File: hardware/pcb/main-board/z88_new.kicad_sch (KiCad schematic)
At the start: 0 parts

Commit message: start next board iteration, add latch and pico power bits
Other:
- added sheet Picos Latch (picos_latch.kicad_sch)
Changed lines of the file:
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@@
 	(title_block
 		(title "Z88R - Z88 Recreated")
-		(date "2024-08-23")
-		(rev "20240823")
+		(date "2025-12-19")
+		(rev "20251219WIP")
 		(company "Fountain and Menadue")
 	)
@@
 				)
 			)
+		)
+	)
+	(sheet
+		(at 50.8 189.23)
+		(size 20.32 3.81)
+		(fields_autoplaced yes)
+		(stroke
+			(width 0.1524)
+			(type solid)
+		)
+		(fill
+			(color 0 0 0 0.0000)
+		)
+		(property "Sheetname" "Picos Latch"
+			(at 50.8 188.5184 0)
+			(effects
+				(font
+					(size 1.27 1.27)
+				)
+				(justify left bottom)
+			)
+		)
+		(property "Sheetfile" "picos_latch.kicad_sch"
+			(at 50.8 193.6246 0)
+			(effects
+				(font
+					(size 1.27 1.27)
+				)
+				(justify left top)
+			)
+		)
+		(instances
+			(project "z88_new"
+				(path "/fdce8012-5f35-4f58-8abb-80214b4af8fe"
+					(page "11")
+				)
+			)

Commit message: make a start on RP2040 to replace the KB pico
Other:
- added sheet KB_RP2040 (kb_rp2040.kicad_sch)
- title: Z88R - Z88 Recreated -> Z88R - Z88 Recreation
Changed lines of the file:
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@@
 	(paper "A4")
 	(title_block
-		(title "Z88R - Z88 Recreated")
-		(date "2025-12-19")
-		(rev "20251219WIP")
+		(title "Z88R - Z88 Recreation")
+		(date "2025-12-30")
+		(rev "20251230WIP")
 		(company "Fountain and Menadue")
 	)
@@
 				)
 			)
+		)
+	)
+	(sheet
+		(at 90.17 187.96)
+		(size 25.4 3.81)
+		(fields_autoplaced yes)
+		(stroke
+			(width 0.1524)
+			(type solid)
+		)
+		(fill
+			(color 0 0 0 0.0000)
+		)
+		(property "Sheetname" "KB_RP2040"
+			(at 90.17 187.2484 0)
+			(effects
+				(font
+					(size 1.27 1.27)
+				)
+				(justify left bottom)
+			)
+		)
+		(property "Sheetfile" "kb_rp2040.kicad_sch"
+			(at 90.17 192.3546 0)
+			(effects
+				(font
+					(size 1.27 1.27)
+				)
+				(justify left top)
+			)
+		)
+		(instances
+			(project "z88_new"
+				(path "/fdce8012-5f35-4f58-8abb-80214b4af8fe"
+					(page "12")
+				)
+			)

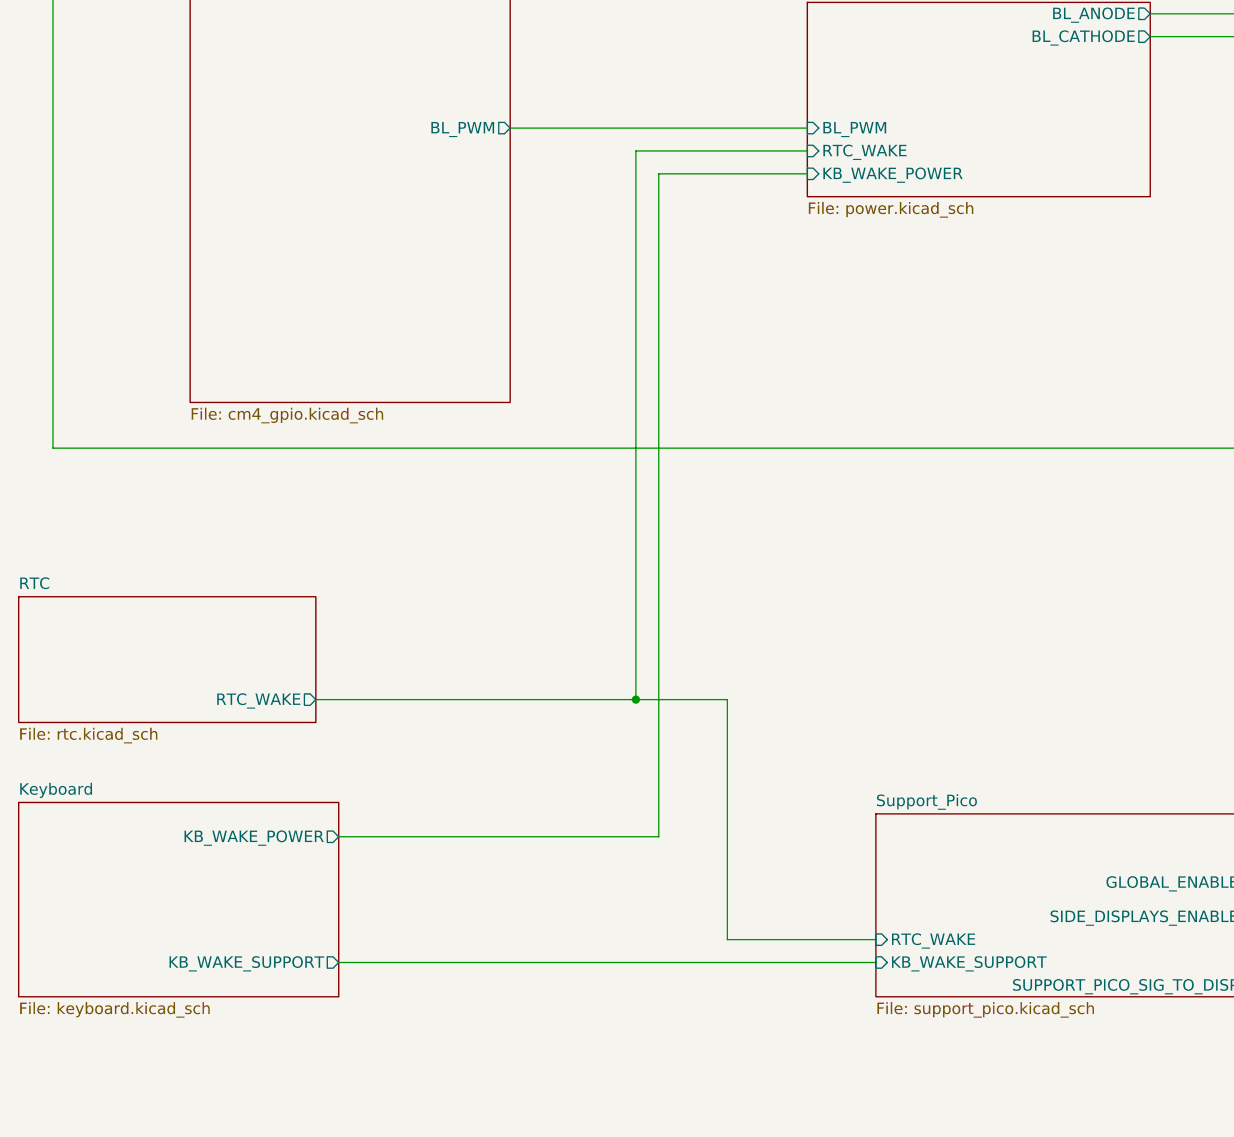
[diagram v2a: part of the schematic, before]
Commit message: more working out of the KB pico replacement
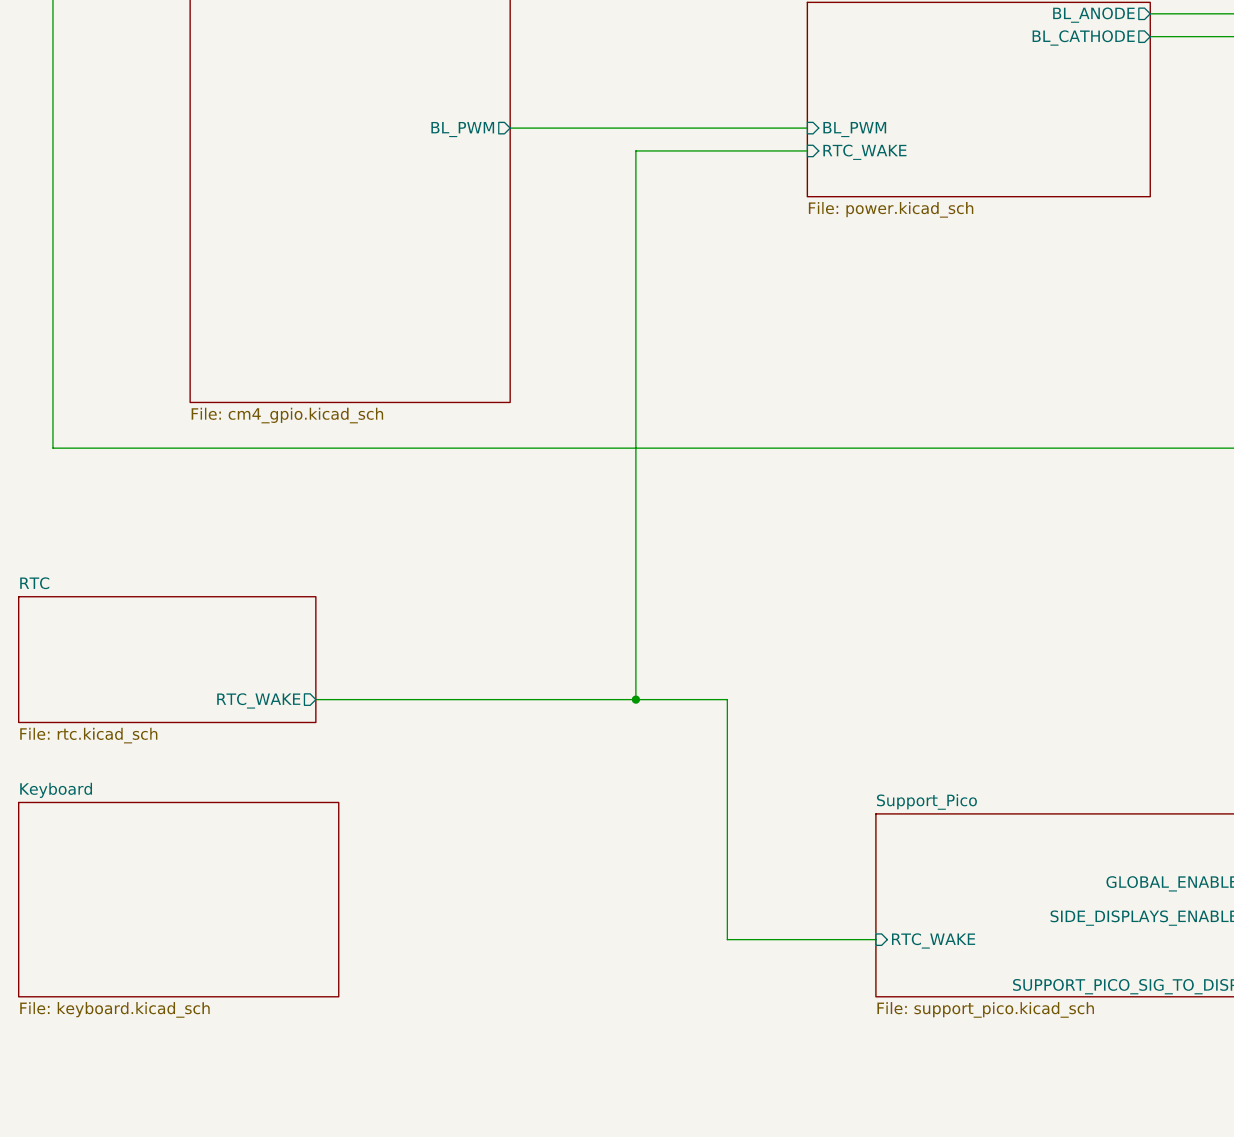
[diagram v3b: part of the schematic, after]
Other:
- sheet Keyboard ports: added none; removed KB_WAKE_POWER, KB_WAKE_SUPPORT
- sheet Power ports: added none; removed KB_WAKE_POWER
- sheet Support_Pico ports: added none; removed KB_WAKE_SUPPORT
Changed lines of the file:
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@@
-	(wire
-		(pts
-			(xy 96.52 58.42) (xy 113.03 58.42)
-		)
-		(stroke
-			(width 0)
-			(type default)
-		)
-	)
-	(wire
-		(pts
-			(xy 60.96 146.05) (xy 120.65 146.05)
-		)
-		(stroke
-			(width 0)
-			(type default)
-		)
-	)
 	(wire
 		(pts
@@
 	(wire
 		(pts
-			(xy 96.52 132.08) (xy 96.52 58.42)
-		)
-		(stroke
-			(width 0)
-			(type default)
-		)
-	)
-	(wire
-		(pts
 			(xy 104.14 143.51) (xy 120.65 143.51)
 		)
@@
 		(pts
 			(xy 93.98 55.88) (xy 93.98 116.84)
-		)
-		(stroke
-			(width 0)
-			(type default)
-		)
-	)
-	(wire
-		(pts
-			(xy 60.96 132.08) (xy 96.52 132.08)
 		)
 		(stroke
@@
 		(pin "RTC_WAKE" input
 			(at 120.65 143.51 180)
-			(effects
-				(font
-					(size 1.27 1.27)
-				)
-				(justify left)
-			)
-		)
-		(pin "KB_WAKE_SUPPORT" input
-			(at 120.65 146.05 180)
 			(effects
 				(font
@@
 			)
 		)
-		(pin "KB_WAKE_SUPPORT" output
-			(at 60.96 146.05 0)
-			(effects
-				(font
-					(size 1.27 1.27)
-				)
-				(justify right)
-			)
-		)
-		(pin "KB_WAKE_POWER" output
-			(at 60.96 132.08 0)
-			(effects
-				(font
-					(size 1.27 1.27)
-				)
-				(justify right)
-			)
-		)
 		(instances
 			(project "z88_new"
@@
 			(effects
 				(font
-					(size 1.27 1.27)
-				)
-				(justify left)
-			)
-		)
-		(pin "KB_WAKE_POWER" input
-			(at 113.03 58.42 180)
-			(effects
-				(font

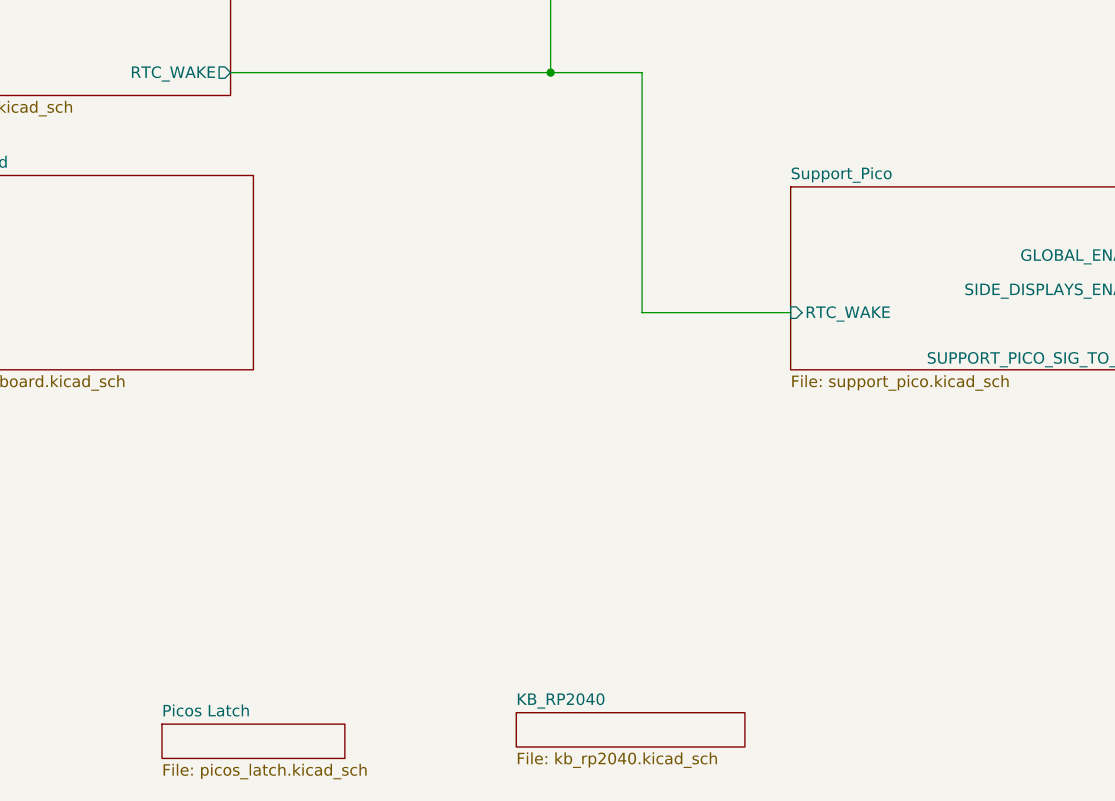
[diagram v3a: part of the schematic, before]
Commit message: start the support pico rp2040 replacement
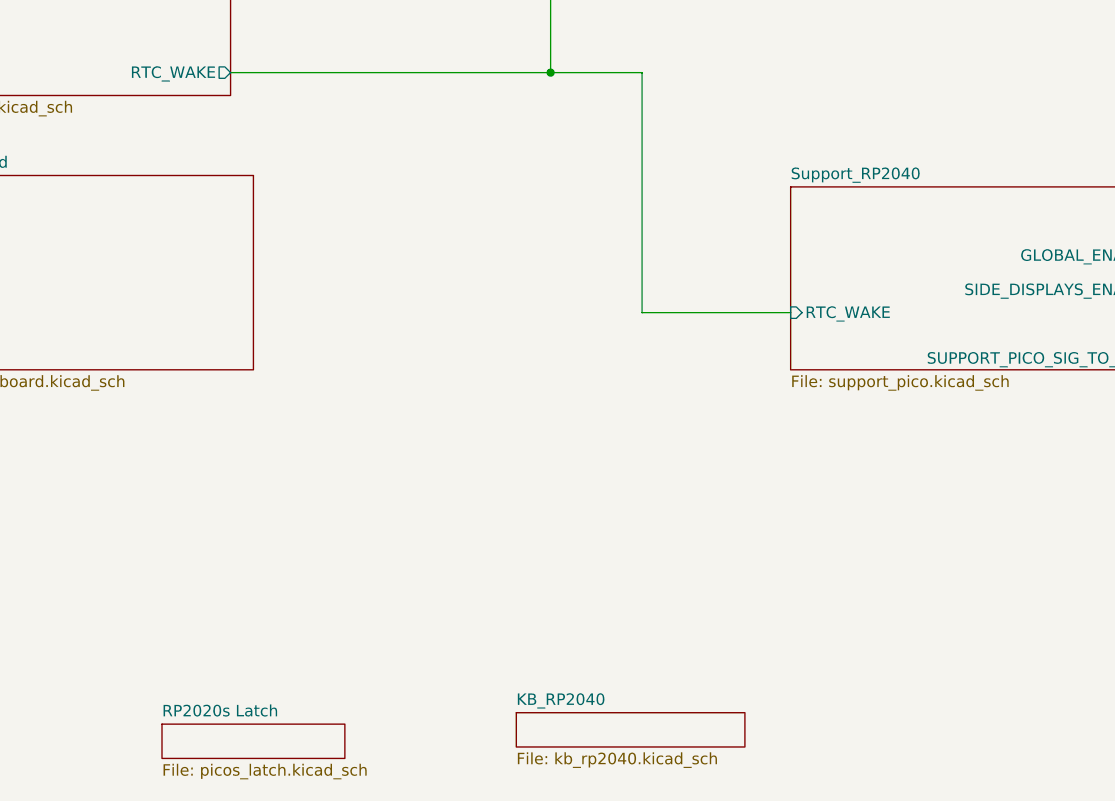
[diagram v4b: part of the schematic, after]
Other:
- sheet Picos Latch renamed RP2020s Latch
- sheet Support_Pico renamed Support_RP2040
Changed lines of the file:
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@@
 	(title_block
 		(title "Z88R - Z88 Recreation")
-		(date "2025-12-30")
-		(rev "20251230WIP")
+		(date "2026-01-01")
+		(rev "20260101WIP")
 		(company "Fountain and Menadue")
 	)
@@
 			(color 0 0 0 0.0000)
 		)
-		(property "Sheetname" "Support_Pico"
+		(property "Sheetname" "Support_RP2040"
 			(at 120.65 128.8284 0)
 			(effects
@@
 			(color 0 0 0 0.0000)
 		)
-		(property "Sheetname" "Picos Latch"
+		(property "Sheetname" "RP2020s Latch"
 			(at 50.8 188.5184 0)
 			(effects

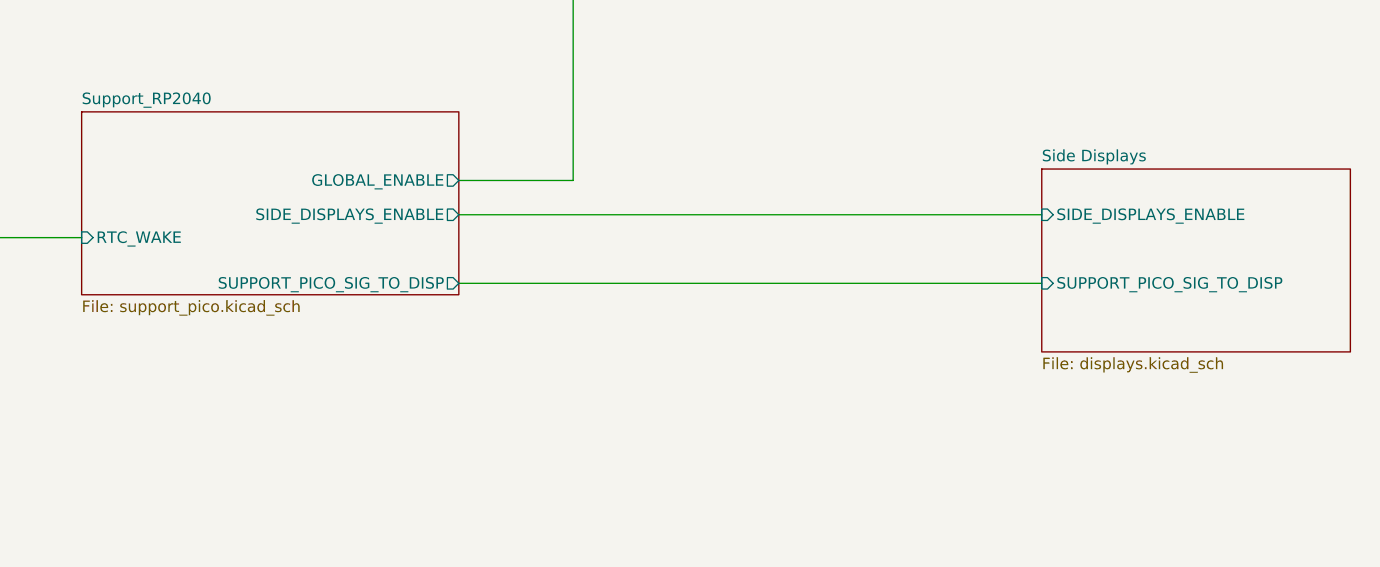
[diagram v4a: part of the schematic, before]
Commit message: rename the pico bits to RP2040, still a few things to check
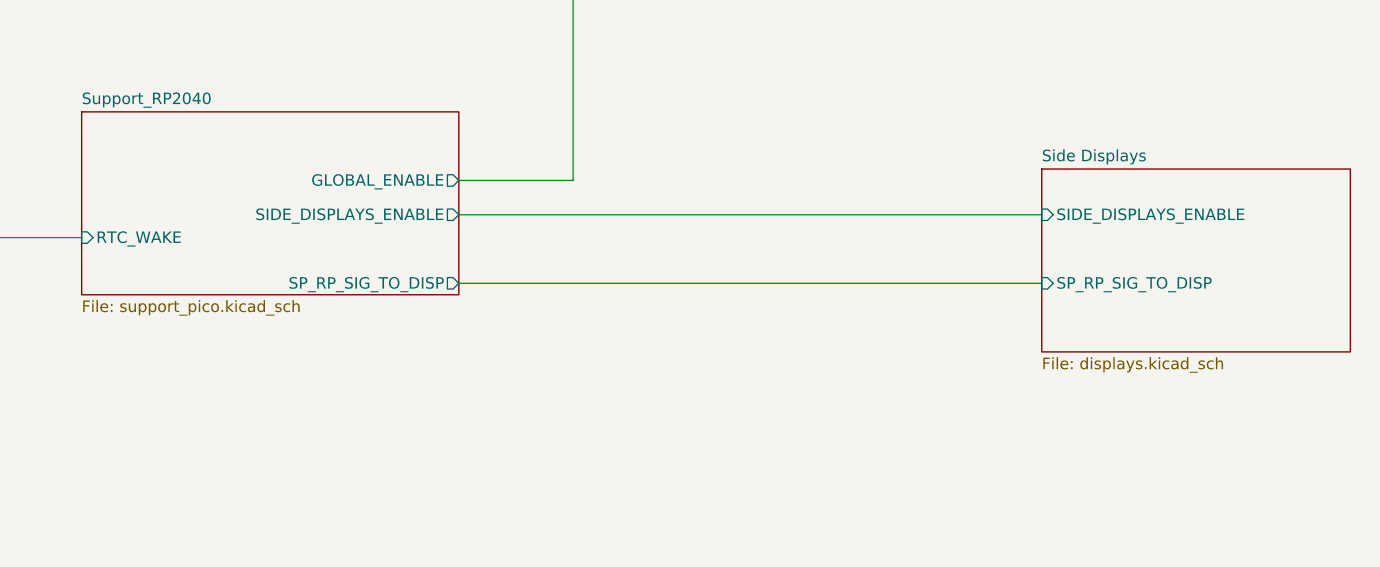
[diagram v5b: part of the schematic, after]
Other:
- sheet Side Displays ports: added SP_RP_SIG_TO_DISP; removed SUPPORT_PICO_SIG_TO_DISP
- sheet Support_RP2040 ports: added SP_RP_SIG_TO_DISP; removed SUPPORT_PICO_SIG_TO_DISP
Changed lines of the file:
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@@
 			)
 		)
-		(pin "SUPPORT_PICO_SIG_TO_DISP" output
+		(pin "SP_RP_SIG_TO_DISP" output
 			(at 162.56 148.59 0)
 			(effects
@@
 			)
 		)
-		(pin "SUPPORT_PICO_SIG_TO_DISP" input
+		(pin "SP_RP_SIG_TO_DISP" input
 			(at 227.33 148.59 180)
 			(effects

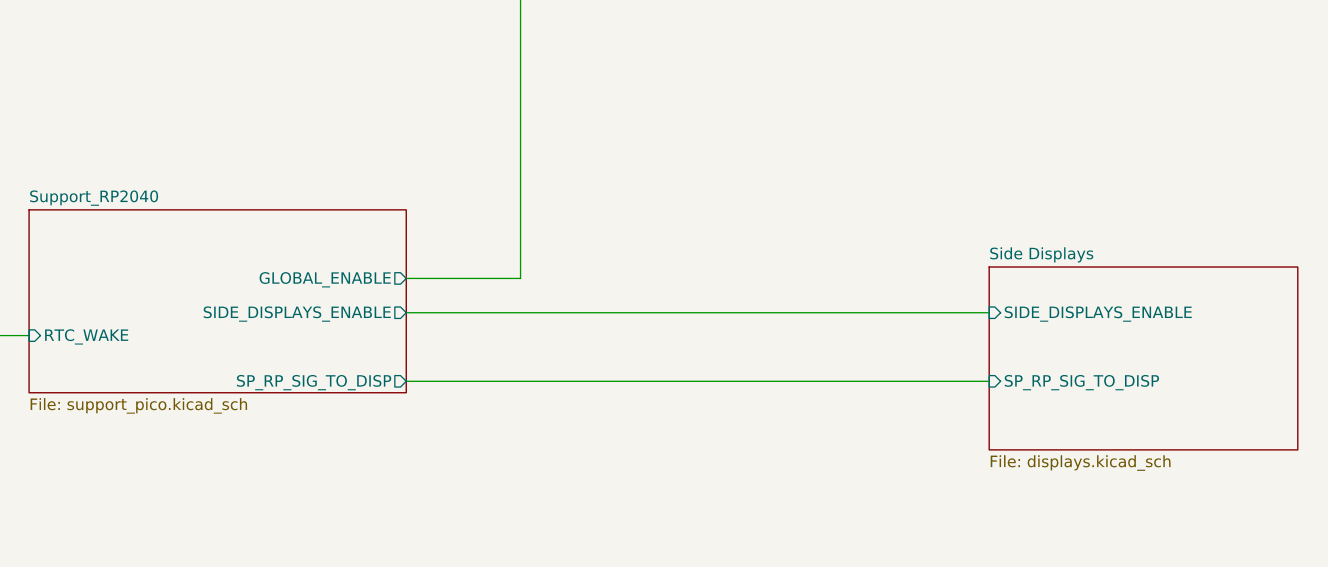
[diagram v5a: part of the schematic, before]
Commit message: rename display board things to application board things
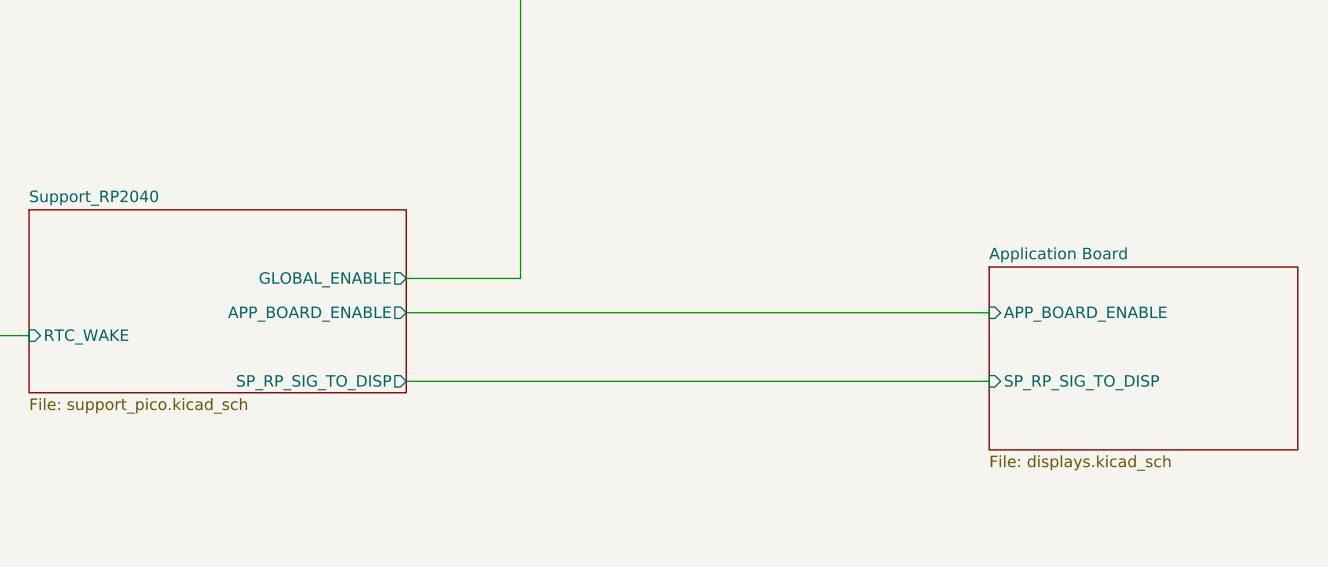
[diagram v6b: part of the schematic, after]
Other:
- sheet Side Displays renamed Application Board
- sheet Application Board ports: added APP_BOARD_ENABLE; removed SIDE_DISPLAYS_ENABLE
- sheet Support_RP2040 ports: added APP_BOARD_ENABLE; removed SIDE_DISPLAYS_ENABLE
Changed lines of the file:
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@@
 			)
 		)
-		(pin "SIDE_DISPLAYS_ENABLE" output
+		(pin "APP_BOARD_ENABLE" output
 			(at 162.56 140.97 0)
 			(effects
@@
 			(color 0 0 0 0.0000)
 		)
-		(property "Sheetname" "Side Displays"
+		(property "Sheetname" "Application Board"
 			(at 227.33 135.1784 0)
 			(effects
@@
 			)
 		)
-		(pin "SIDE_DISPLAYS_ENABLE" input
+		(pin "APP_BOARD_ENABLE" input
 			(at 227.33 140.97 180)
 			(effects
